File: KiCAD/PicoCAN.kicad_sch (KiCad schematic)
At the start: 52 parts, among them J1 USB_C_Receptacle_USB2.0_14P, J2 Conn_01x20, J3 Conn_01x20, J4 Conn_01x02, J5 Screw_Terminal_01x03 (C381777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, J7 Conn_01x02, SW1 SW_Push, U1 RP2040, U2 MCP1700x-330xxTT, U3 W25Q16JVUXIQ, U4 MCP25625-x-SS (C481365), Y1 12 MHz Crystal_GND24 (C9002), Y2 16 MHz Crystal_GND24 (C13738)

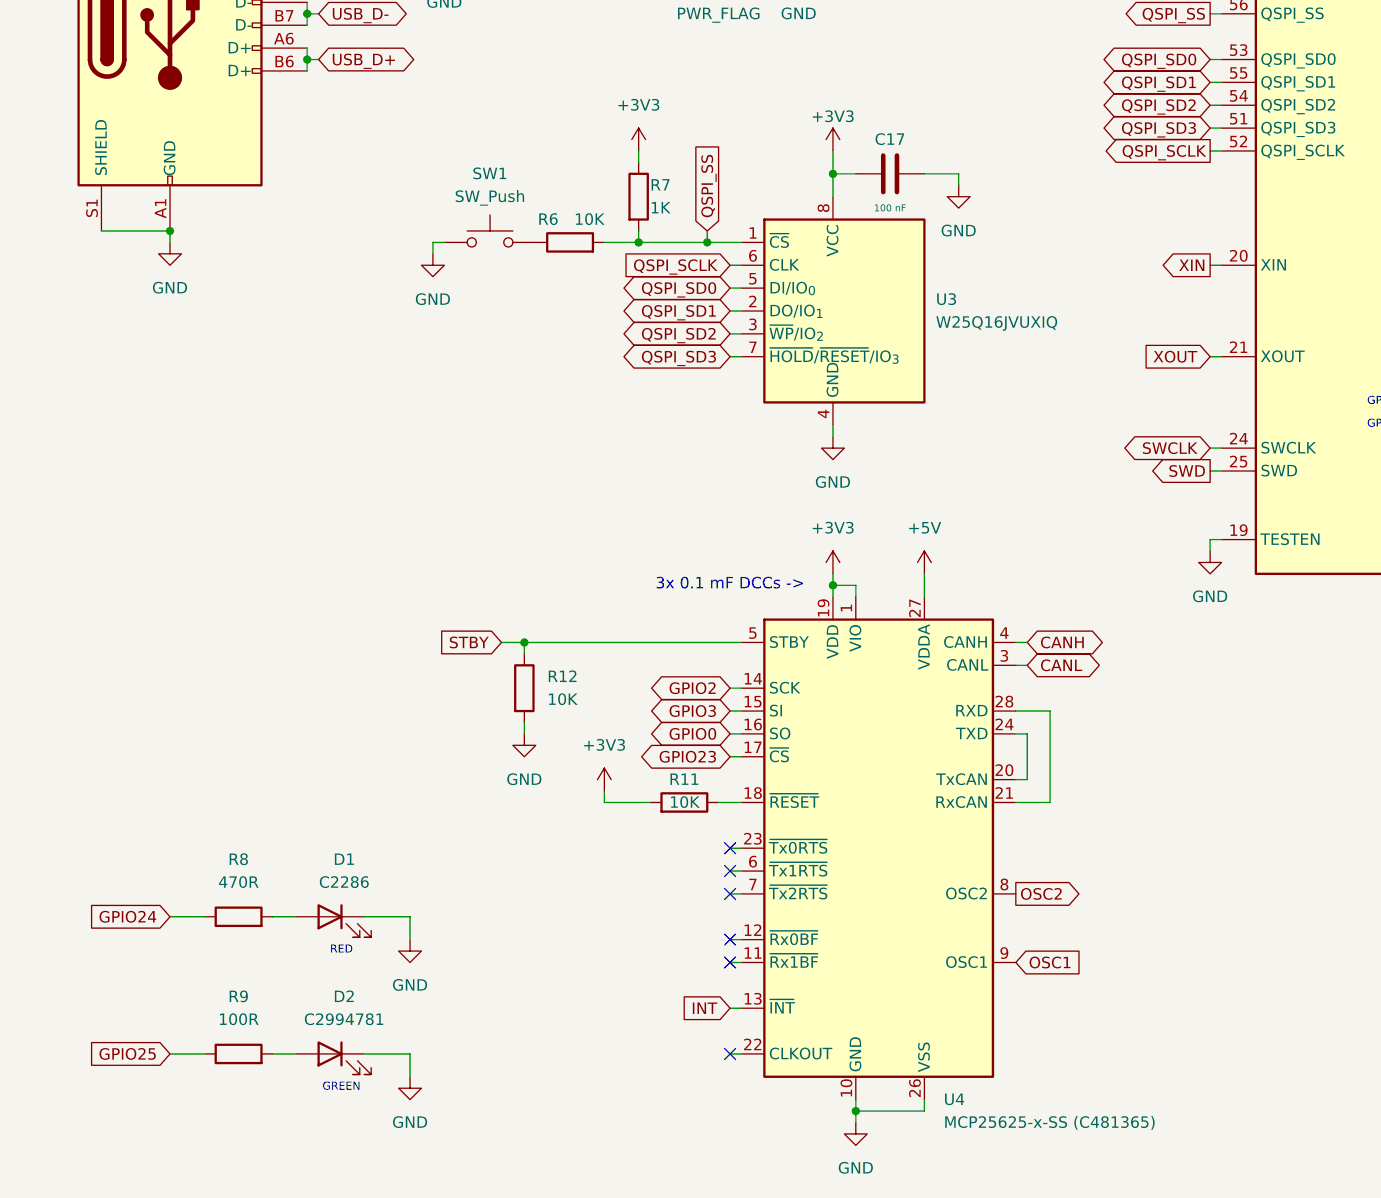
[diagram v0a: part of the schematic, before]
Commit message: MCP25625 issue fixed by rewire
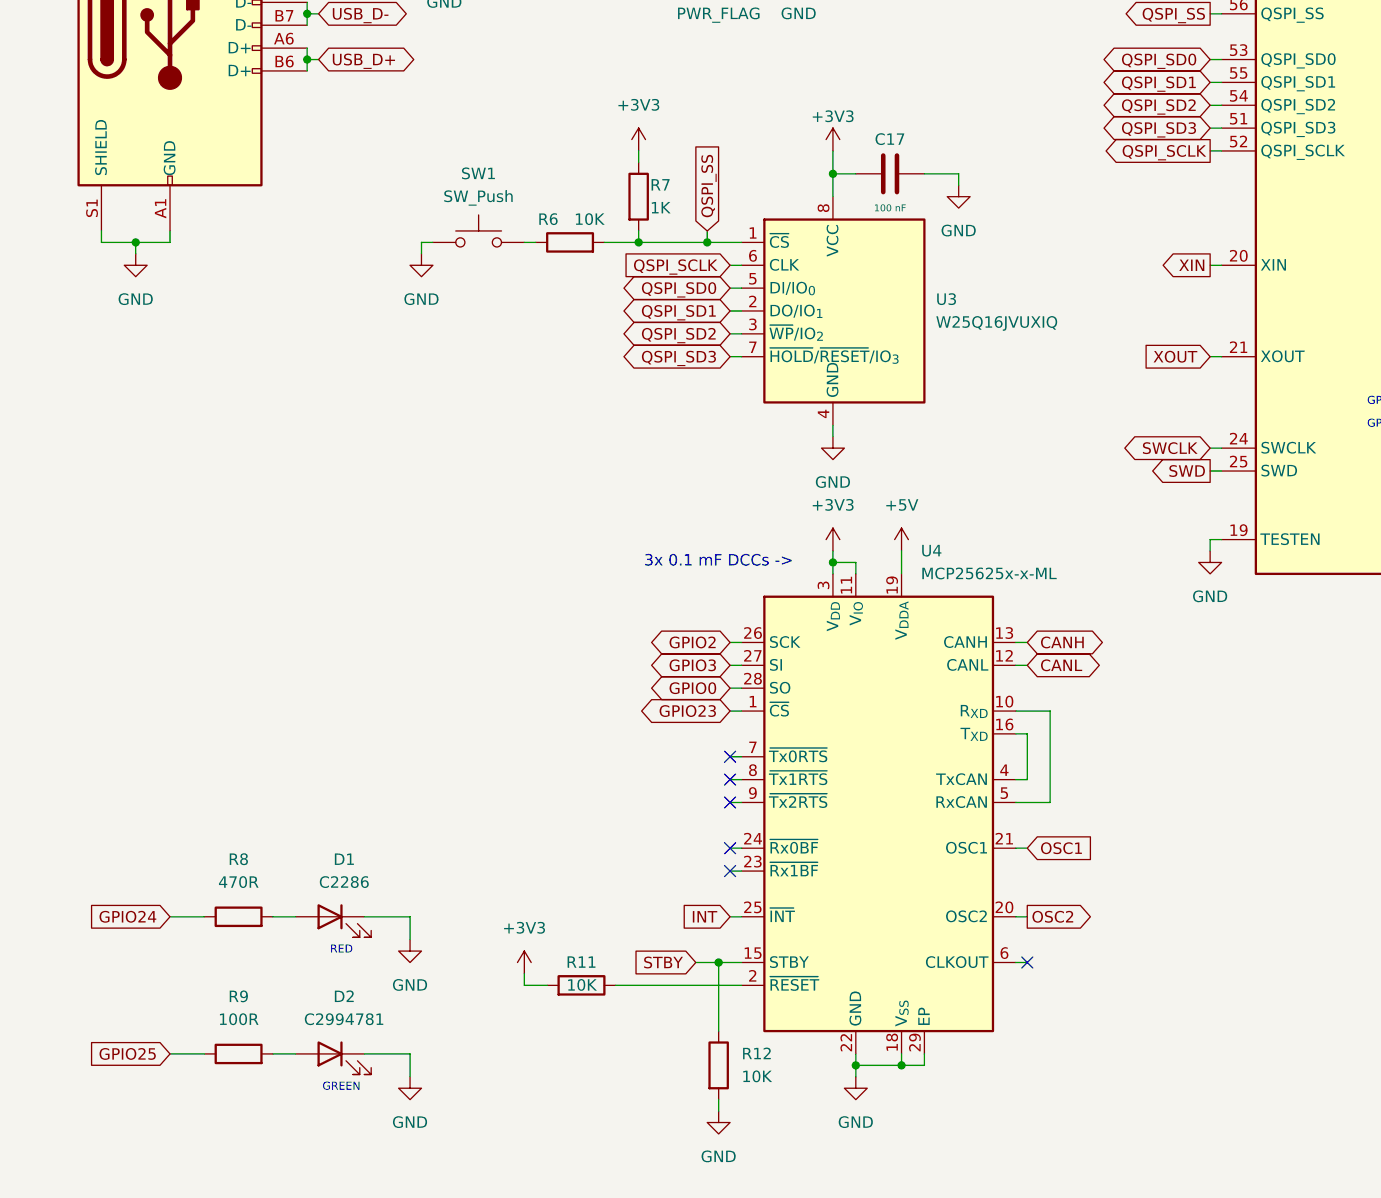
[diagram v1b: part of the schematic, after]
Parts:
- removed U4: MCP25625-x-SS (C481365), easyeda2kicad:QFN-28_L6.0-W6.0-P0.65-BL-EP, symbol Interface_CAN_LIN:MCP25625-x-SS
- added U4: MCP25625x-x-ML, Package_DFN_QFN:QFN-28-1EP_6x6mm_P0.65mm_EP4.25x4.25mm, symbol Interface_CAN_LIN:MCP25625x-x-ML
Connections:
- net +3V3: now also U4.11 (V_{IO}), U4.3 (V_{DD})
- net +5V: now also U4.19 (V_{DDA})
- net CANH: now also U4.13 (CANH)
- net CANL: now also U4.12 (CANL)
- net GND: now also U4.18 (V_{SS}), U4.22 (GND), U4.29 (EP)
- net GPIO0: now also U4.28 (SO)
- net GPIO2: now also U4.26 (SCK)
- net GPIO23: now also U4.1 (~{CS})
- net GPIO3: now also U4.27 (SI)
- net INT: now also U4.25 (~{INT})
- net OSC1: now also U4.21 (OSC1)
- net OSC2: now also U4.20 (OSC2)
- net STBY: now also U4.15 (STBY)
- net at R11.1: now also U4.2 (~{RESET})
- new net: U4.10 (R_{XD}), U4.5 (RxCAN)
- new net: U4.16 (T_{XD}), U4.4 (TxCAN)
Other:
- moved on the sheet: R11, R12, SW1

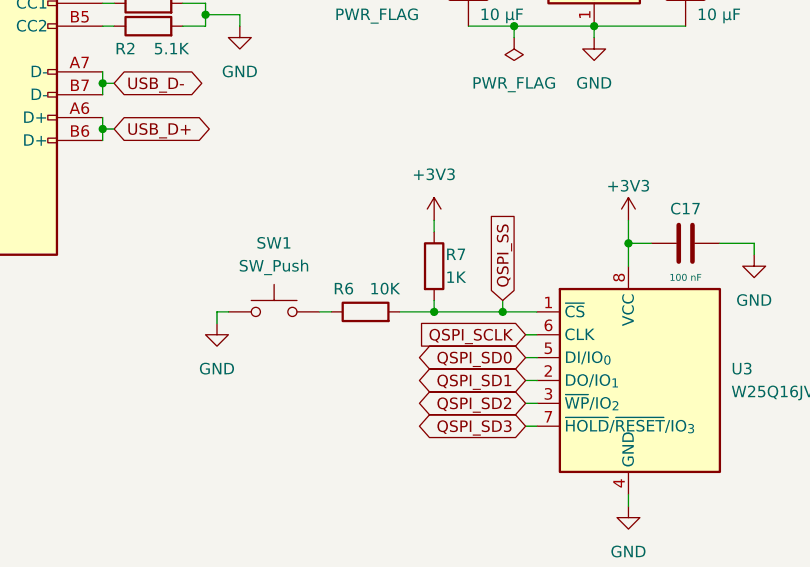
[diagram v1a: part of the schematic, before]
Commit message: Swap R6 and R7
Fixes issue of button not activating BOOTSEL mode
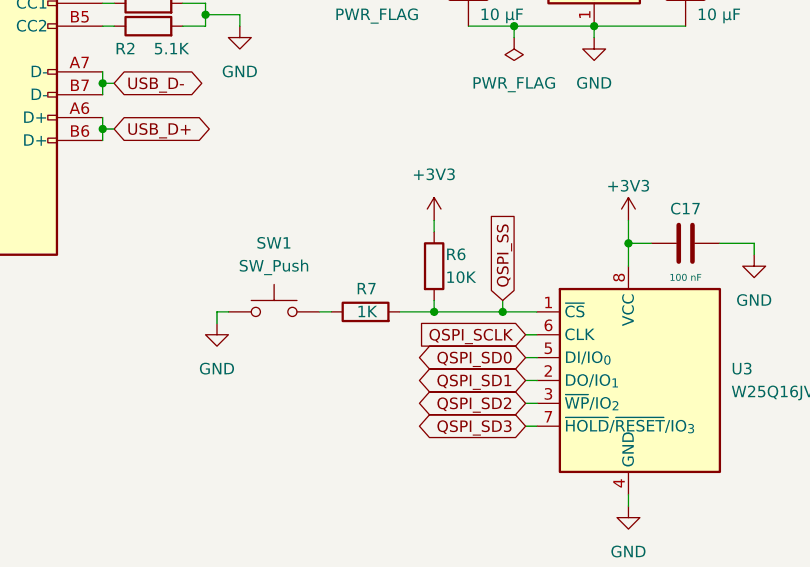
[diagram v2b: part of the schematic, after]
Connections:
- net +3V3: now also R6.1; no longer R7.1
- net at SW1.2: now also R7.1; no longer R6.1
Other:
- moved on the sheet: R6, R7
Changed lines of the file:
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@@
 	(symbol
 		(lib_id "Device:R")
-		(at 73.66 91.44 90)
+		(at 81.28 86.36 0)
 		(unit 1)
 		(body_style 1)
@@
 		(dnp no)
 		(property "Reference" "R6"
-			(at 72.39 88.9 90)
+			(at 82.55 85.09 0)
 			(show_name no)
 			(do_not_autoplace no)
@@
 		)
 		(property "Value" "10K"
-			(at 77.47 88.9 90)
+			(at 82.55 87.63 0)
 			(show_name no)
 			(do_not_autoplace no)
@@
 		)
 		(property "Footprint" "Resistor_SMD:R_0402_1005Metric"
-			(at 73.66 93.218 90)
+			(at 79.502 86.36 90)
 			(hide yes)
 			(show_name no)
@@
 		)
 		(property "Datasheet" ""
-			(at 73.66 91.44 0)
+			(at 81.28 86.36 0)
 			(hide yes)
 			(show_name no)
@@
 		)
 		(property "Description" "Resistor"
-			(at 73.66 91.44 0)
+			(at 81.28 86.36 0)
 			(hide yes)
 			(show_name no)
@@
 		)
 		(property "MPN" "C25744"
-			(at 73.66 91.44 90)
+			(at 81.28 86.36 90)
 			(hide yes)
 			(show_name no)
@@
 		)
 		(property "Notes" "Basic: C25744, Extended: C176114"
-			(at 73.66 91.44 90)
+			(at 81.28 86.36 90)
 			(hide yes)
 			(show_name no)
@@
 	(symbol
 		(lib_id "Device:R")
-		(at 81.28 86.36 0)
+		(at 73.66 91.44 90)
 		(unit 1)
 		(body_style 1)
@@
 		(dnp no)
 		(property "Reference" "R7"
-			(at 82.55 85.09 0)
+			(at 74.93 88.9 90)
 			(show_name no)
 			(do_not_autoplace no)
@@
 		)
 		(property "Value" "1K"
-			(at 82.55 87.63 0)
+			(at 74.93 91.44 90)
 			(show_name no)
 			(do_not_autoplace no)
@@
 		)
 		(property "Footprint" "Resistor_SMD:R_0402_1005Metric"
-			(at 79.502 86.36 90)
+			(at 73.66 93.218 90)
 			(hide yes)
 			(show_name no)
@@
 		)
 		(property "Datasheet" ""
-			(at 81.28 86.36 0)
+			(at 73.66 91.44 0)
 			(hide yes)
 			(show_name no)
@@
 		)
 		(property "Description" "Resistor"
-			(at 81.28 86.36 0)
+			(at 73.66 91.44 0)
 			(hide yes)
 			(show_name no)
@@
 		)
 		(property "MPN" "C11702"
-			(at 81.28 86.36 0)
+			(at 73.66 91.44 0)
 			(hide yes)
 			(show_name no)
@@
 		)
 		(property "Notes" ""
-			(at 81.28 86.36 0)
+			(at 73.66 91.44 0)
 			(hide yes)
 			(show_name no)
